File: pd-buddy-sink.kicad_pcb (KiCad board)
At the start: 2 copper layers, 48 x 26 mm, 38 parts, among them J1 5-20 V⎓, P1 12401548E4#2A, P2 SWD, Q1 MMBT2222ALT1G, Q2 DMP4015SSS, SW1 Boot, SW2 Setup, U1 AP2204R-3.3TRG1, U2 STM32F072CBTx, U3 FUSB302B

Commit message: Changed USB connector to SMD version
There's now quite a bit of stuff located under the USB connector.  A lot
of manufacturers mark that area as a keep-out zone, but luckily,
Amphenol is not one of them.
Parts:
- P1: value 12401548E4#2A -> 12401610E4#2A; footprint pd-buddy:Amphenol-12401548E4#2A -> pd-buddy:Amphenol-12401610E4#2A
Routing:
- net /Microcontroller/D-: track 18.8 -> 24.7 mm, vias 3 -> 4
- net /Microcontroller/D+: track 18.8 -> 24.3 mm, vias 3 -> 4
- net VBUS: track 34.8 -> 39.3 mm, vias 26 -> 32
- net /PD PHY/CC2: track 17.3 -> 19.7 mm
- net GND: track 107.9 -> 109.2 mm, vias 27 -> 33

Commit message: Changed R9 to 100 kΩ
As it was, it wasted around 85 mW whenever the output was turned on at
20 V.  That's a silly waste of power.  A 100 kΩ pullup works just fine,
so I changed it.  Now there's only 4 mW wasted, so I'm happy.
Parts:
- R9: value 4.7kΩ -> 100kΩ
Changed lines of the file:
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@@
       (effects (font (size 0.8 0.8) (thickness 0.15)))
     )
-    (fp_text value 4.7kΩ (at 0 1.75 180) (layer F.Fab)
+    (fp_text value 100kΩ (at 0 1.75 180) (layer F.Fab)
       (effects (font (size 1 1) (thickness 0.15)))
     )

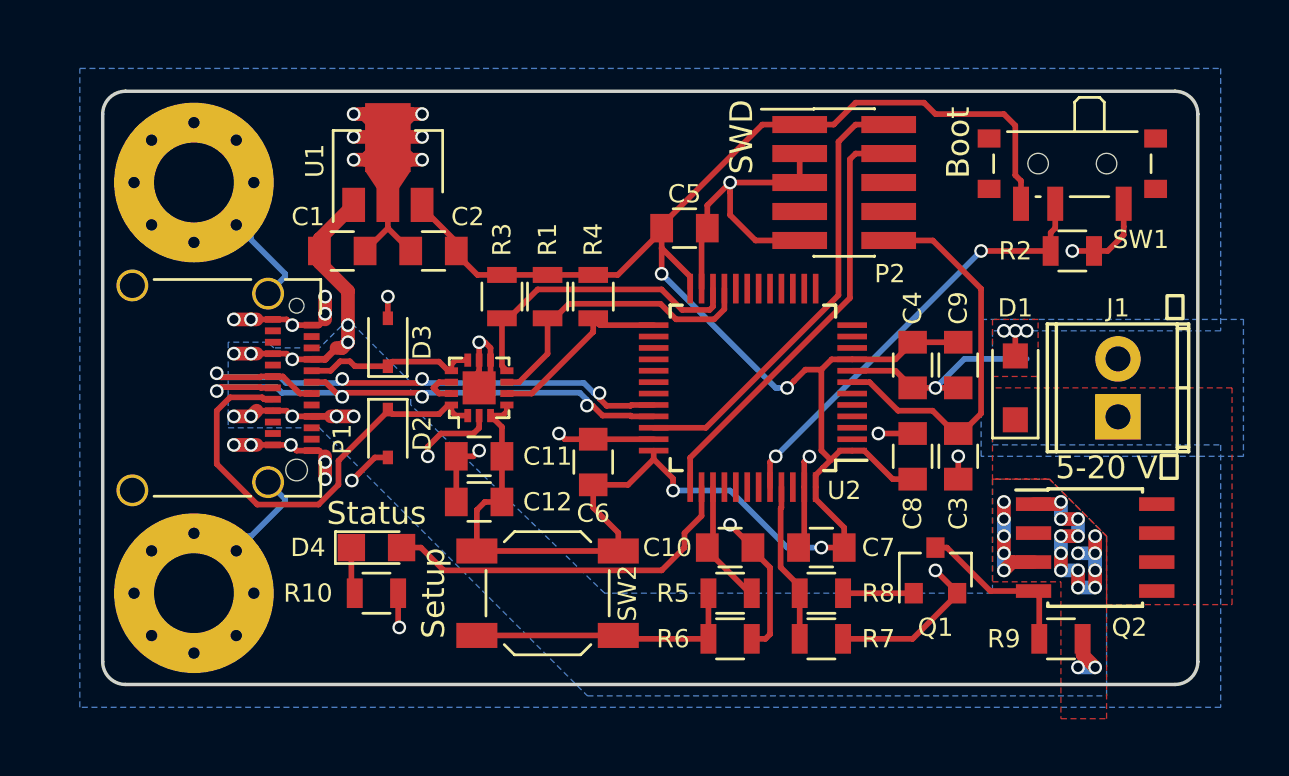
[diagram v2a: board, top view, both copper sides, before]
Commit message: 4-layer board with smaller components
This is a major change!  Almost all the components have changed to
smaller versions, with 0603 and 0402 passives and a QFN microcontroller.
The board now has four layers, with internal layers used for VBUS and
GND.  The board now measures a mere 25×30 mm!  The SWD header and Boot
switch footprints have been moved to the bottom to help with this
shrinkage.  Two test points were added to the bottom as well to make it
possible to power the board without using the USB connector.  The
mounting holes are now slightly smaller (better sized for M3), and only
17 mm apart instead of the old 18 mm.

To sum up, everything is smaller and that's almost entirely a good
thing, except now it's not really possible to build one by hand.
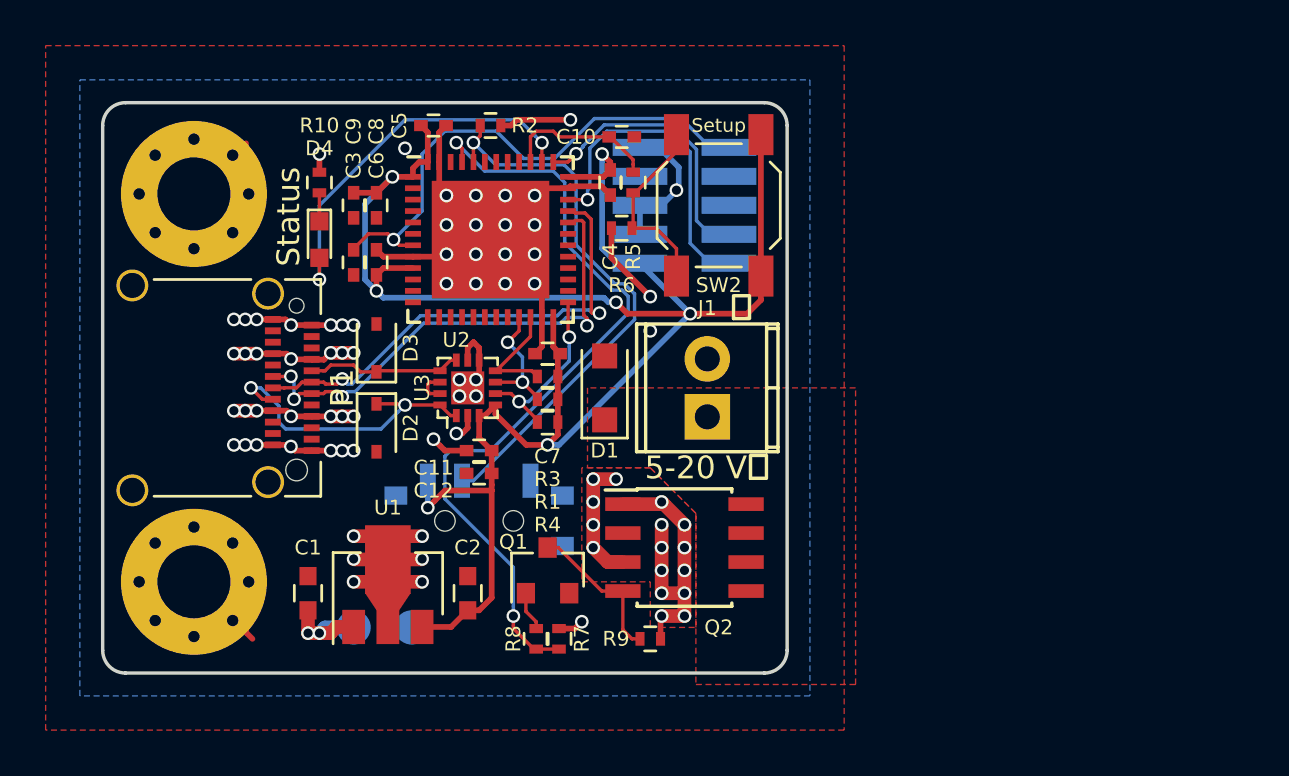
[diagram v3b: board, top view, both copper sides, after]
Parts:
- added TP1: VBUS, Measurement_Points:Measurement_Point_Round-SMD-Pad_Small, B.Cu at (92.5, 80.5)
- added TP2: GND, Measurement_Points:Measurement_Point_Round-SMD-Pad_Small, B.Cu at (95.0, 80.5)
- C1: value 1.0μF -> 1.0μF 25V; footprint Capacitors_SMD:C_0805 -> Capacitors_SMD:C_0603
- C10, C11, C12, C3, C4, C5, C6, C7, C8, C9: footprint Capacitors_SMD:C_0805 -> Capacitors_SMD:C_0402
- C2: footprint Capacitors_SMD:C_0805 -> Capacitors_SMD:C_0603
- D4: footprint LEDs:LED_0805 -> LEDs:LED_0603
- MK1, MK2: value 3.5mm -> M3; footprint Mounting_Holes:MountingHole_3.5mm_Pad_Via -> Mounting_Holes:MountingHole_3.2mm_M3_Pad_Via
- P2, SW1: moved to B.Cu
- R1, R10, R2, R3, R4, R5, R6, R7, R8, R9: footprint Resistors_SMD:R_0805 -> Resistors_SMD:R_0402
- U2: value STM32F072CBTx -> STM32F072C8Ux; footprint Housings_QFP:LQFP-48_7x7mm_Pitch0.5mm -> Housings_DFN_QFN:QFN-48-1EP_7x7mm_Pitch0.5mm
- moved SW1 30.0 mm to (98.0, 75.5)
- moved C3 27.8 mm to (92.5, 64.5)
- moved C9 27.4 mm to (92.5, 62.0)
- moved R2 26.1 mm to (98.5, 58.5)
- moved C8 25.9 mm to (93.5, 62.0), turned to 270 degrees
- moved C10 18.6 mm to (104.2, 59.0)
- moved R6 18.6 mm to (104.2, 63.0), turned to 180 degrees
- moved SW2 18.6 mm to (108.5, 62.0), turned to 270 degrees
- moved U1 18.5 mm to (94.0, 79.0)
- moved R5 18.5 mm to (104.8, 61.0), turned to 90 degrees
- moved R10 18.2 mm to (91.0, 61.0), turned to 90 degrees
- moved D1 18.0 mm to (103.5, 70.0)
- moved J1 18.0 mm to (108.0, 71.3)
- moved Q2 18.0 mm to (107.0, 77.0)
- moved R9 18.0 mm to (105.5, 81.0)
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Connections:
- net /Microcontroller/NOPWR renamed /Microcontroller/STATUS
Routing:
- net GND: track 109.2 -> 68.4 mm, vias 33 -> 48
- net /Microcontroller/OUT_CTRL: track 7.01 -> 35.3 mm, vias 0 -> 2
- net +3V3: track 99.6 -> 85.5 mm, vias 4 -> 7
- net /Microcontroller/SDA: track 13.4 -> 4.94 mm
- net /Microcontroller/SCL: track 13.2 -> 5.53 mm, vias 0 -> 2
- net /Microcontroller/SWCLK: track 19.1 -> 12.3 mm, vias 0 -> 1
- net /PD PHY/CC2: track 19.7 -> 13.3 mm, vias 0 -> 2
- net /Microcontroller/nRST: track 16.7 -> 23.0 mm, vias 0 -> 1
- net /Microcontroller/BOOT: track 19.4 -> 24.9 mm, vias 2 -> 1
- net /Microcontroller/SWDIO: track 19.7 -> 14.3 mm, vias 0 -> 1
- net Net-(R5-Pad1): track 12.2 -> 8.49 mm
- net VBUS: track 39.3 -> 36.2 mm, vias 32 -> 33
- net /Microcontroller/D-: track 24.7 -> 22.0 mm
- net /Microcontroller/D+: track 24.3 -> 21.7 mm, vias 4 -> 2
- net Net-(Q1-Pad1): track 3.10 -> 1.74 mm
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- added copper zone on In2.Cu, net GND
- added copper zone on In1.Cu, net VBUS
- removed copper zone on B.Cu, net VBUS
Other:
- board size 48 x 26 mm -> 30 x 25 mm
- copper layers 2 -> 4
- net class Default: clearance 0.16 -> 0.127; trace_width 0.25 -> 0.15
- net class Power: trace_width 1.5 -> 0.6
- net class Power_Small: trace_width 0.6 -> 0.25
- rule pad_to_mask_clearance: 0.125 -> 0.0635
- rule trace_clearance: 0.16 -> 0.127
- rule trace_min: 0.2 -> 0.127
- rule via_min_drill: 0.3 -> 0.254
- rule via_min_size: 0.4 -> 0.4572

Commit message: Added fiducials to board top
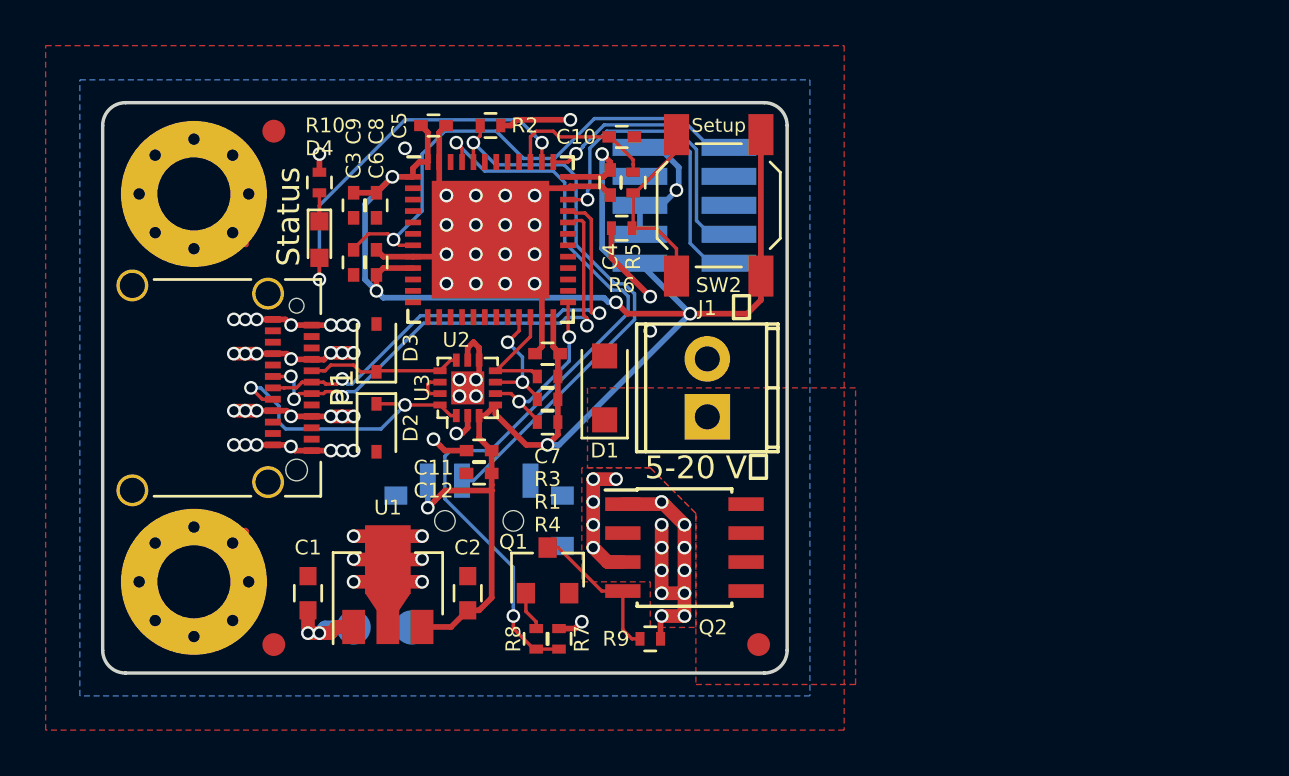
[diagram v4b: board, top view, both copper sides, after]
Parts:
- added FID1: Fiducial_1mm_Dia_2.54mm_Outer_CopperTop, Fiducials:Fiducial_1mm_Dia_2.54mm_Outer_CopperTop, F.Cu at (89.0, 58.8)
- added FID2: Fiducial_1mm_Dia_2.54mm_Outer_CopperTop, Fiducials:Fiducial_1mm_Dia_2.54mm_Outer_CopperTop, F.Cu at (89.0, 81.2)
- added FID3: Fiducial_1mm_Dia_2.54mm_Outer_CopperTop, Fiducials:Fiducial_1mm_Dia_2.54mm_Outer_CopperTop, F.Cu at (110.2, 81.2)
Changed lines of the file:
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@@
     (links 138)
     (no_connects 0)
-    (area 78.565 55 114.500001 85.71)
+    (area 81.424999 57.424999 111.575001 82.575001)
     (thickness 1.6)
     (drawings 10)
     (tracks 529)
     (zones 0)
-    (modules 40)
+    (modules 43)
     (nets 64)
   )
@@
     (add_net GND)
   )
+  (module Fiducials:Fiducial_1mm_Dia_2.54mm_Outer_CopperTop (layer F.Cu)
+    (at 110.25 81.25)
+    (descr "Circular Fiducial, 1mm bare copper top; 2.54mm keepout")
+    (tags marker)
+    (attr virtual)
+    (fp_text reference FID3 (at 3.4 0.7) (layer F.SilkS) hide
+      (effects (font (size 1 1) (thickness 0.15)))
+    )
+    (fp_text value Fiducial_1mm_Dia_2.54mm_Outer_CopperTop (at 0 -1.8) (layer F.Fab)
+      (effects (font (size 1 1) (thickness 0.15)))
+    )
+    (fp_circle (center 0 0) (end 1.55 0) (layer F.CrtYd) (width 0.05))
+    (pad ~ smd circle (at 0 0) (size 1 1) (layers F.Cu F.Mask)
+      (solder_mask_margin 0.77) (clearance 0.77))
+  )
+  (module Fiducials:Fiducial_1mm_Dia_2.54mm_Outer_CopperTop (layer F.Cu)
+    (at 89 81.25)
+    (descr "Circular Fiducial, 1mm bare copper top; 2.54mm keepout")
+    (tags marker)
+    (attr virtual)
+    (fp_text reference FID2 (at 3.4 0.7) (layer F.SilkS) hide
+      (effects (font (size 1 1) (thickness 0.15)))
+    )
+    (fp_text value Fiducial_1mm_Dia_2.54mm_Outer_CopperTop (at 0 -1.8) (layer F.Fab)
+      (effects (font (size 1 1) (thickness 0.15)))
+    )
+    (fp_circle (center 0 0) (end 1.55 0) (layer F.CrtYd) (width 0.05))
+    (pad ~ smd circle (at 0 0) (size 1 1) (layers F.Cu F.Mask)
+      (solder_mask_margin 0.77) (clearance 0.77))
+  )
   (module Housings_DFN_QFN:QFN-48-1EP_7x7mm_Pitch0.5mm (layer F.Cu)
     (at 98.5 63.5)
@@
     (tags "SOIC 1.27")
     (attr smd)
-    (fp_text reference Q2 (at 1.5 3.5) (layer F.SilkS)
+    (fp_text reference Q2 (at 1.25 3.5) (layer F.SilkS)
       (effects (font (size 0.65 0.65) (thickness 0.12)))
     )
@@
     (tags "resistor 0402")
     (attr smd)
-    (fp_text reference R10 (at 2.5 0 180) (layer F.SilkS)
+    (fp_text reference R10 (at 2.5 0.25 180) (layer F.SilkS)
       (effects (font (size 0.65 0.65) (thickness 0.12)))
     )
@@
     (pad B12 smd rect (at -3 1.04 270) (size 0.3 0.7) (layers F.Cu F.Paste F.Mask)
       (net 2 GND))
+  )
+  (module Fiducials:Fiducial_1mm_Dia_2.54mm_Outer_CopperTop (layer F.Cu)
+    (at 89 58.75)
+    (descr "Circular Fiducial, 1mm bare copper top; 2.54mm keepout")
+    (tags marker)
+    (attr virtual)
+    (fp_text reference FID1 (at 3.4 0.7) (layer F.SilkS) hide
+      (effects (font (size 1 1) (thickness 0.15)))
+    )
+    (fp_text value Fiducial_1mm_Dia_2.54mm_Outer_CopperTop (at 0 -1.8) (layer F.Fab)
+      (effects (font (size 1 1) (thickness 0.15)))
+    )
+    (fp_circle (center 0 0) (end 1.55 0) (layer F.CrtYd) (width 0.05))
+    (pad ~ smd circle (at 0 0) (size 1 1) (layers F.Cu F.Mask)
+      (solder_mask_margin 0.77) (clearance 0.77))
   )
   (gr_text "PD Buddy Sink v0.3" (at 110.75 81.25) (layer B.Mask)
@@
   (segment (start 88.96 68.5) (end 88.25 68.5) (width 0.25) (layer F.Cu) (net 1))
   (via (at 88.25 68.5) (size 0.6) (drill 0.4) (layers F.Cu B.Cu) (net 1))
+  (segment (start 85.5 61.5) (end 86.365802 61.5) (width 0.25) (layer F.Cu) (net 2))
+  (segment (start 86.365802 61.5) (end 87.782057 62.916255) (width 0.25) (layer F.Cu) (net 2))
+  (segment (start 87.782057 62.916255) (end 87.782057 63.717943) (width 0.25) (layer F.Cu) (net 2))
+  (segment (start 85.5 78.5) (end 86.365802 78.5) (width 0.25) (layer F.Cu) (net 2))
+  (segment (start 86.365802 78.5) (end 87.782057 77.083745) (width 0.25) (layer F.Cu) (net 2))
+  (segment (start 87.782057 77.083745) (end 87.782057 76.282057) (width 0.25) (layer F.Cu) (net 2))
+  (segment (start 87.782057 76.282057) (end 87.75 76.25) (width 0.25) (layer F.Cu) (net 2))
   (via (at 92.5 67.25) (size 0.6) (drill 0.4) (layers F.Cu B.Cu) (net 2))
   (segment (start 92 67.25) (end 92.5 67.25) (width 0.25) (layer F.Cu) (net 2))
@@
   (segment (start 95.39375 59.5) (end 94.75 59.5) (width 0.25) (layer In2.Cu) (net 2))
   (via (at 94.75 59.5) (size 0.6) (drill 0.4) (layers F.Cu B.Cu) (net 2))
-  (segment (start 85.5 61.5) (end 86.365802 61.5) (width 0.25) (layer F.Cu) (net 2))
-  (segment (start 86.365802 61.5) (end 87.782057 60.083745) (width 0.25) (layer F.Cu) (net 2))
-  (segment (start 87.782057 60.083745) (end 87.782057 59.282057) (width 0.25) (layer F.Cu) (net 2))
-  (segment (start 87.782057 80.717943) (end 88.064114 81) (width 0.25) (layer F.Cu) (net 2))
-  (segment (start 85.5 78.5) (end 86.365802 78.5) (width 0.25) (layer F.Cu) (net 2))
-  (segment (start 86.365802 78.5) (end 87.782057 79.916255) (width 0.25) (layer F.Cu) (net 2))
-  (segment (start 87.782057 79.916255) (end 87.782057 80.717943) (width 0.25) (layer F.Cu) (net 2))
   (segment (start 92 72.75) (end 92.5 72.75) (width 0.25) (layer F.Cu) (net 2))
   (via (at 92.5 72.75) (size 0.6) (drill 0.4) (layers F.Cu B.Cu) (net 2))
